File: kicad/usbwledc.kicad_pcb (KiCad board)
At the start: 2 copper layers, 30 x 35 mm, 31 parts, among them J1 5V PAD, J10 USB_C_Receptacle_USB2.0, J2 D1 PAD, J3 GND PAD, J4 5V PAD, J5 D2 PAD, J6 GND PAD, J7 Accessories, SW1 FLASH_SW, U1 CH340N, U2 AMS1117-3.3, U3 ESP32-WROOM-32

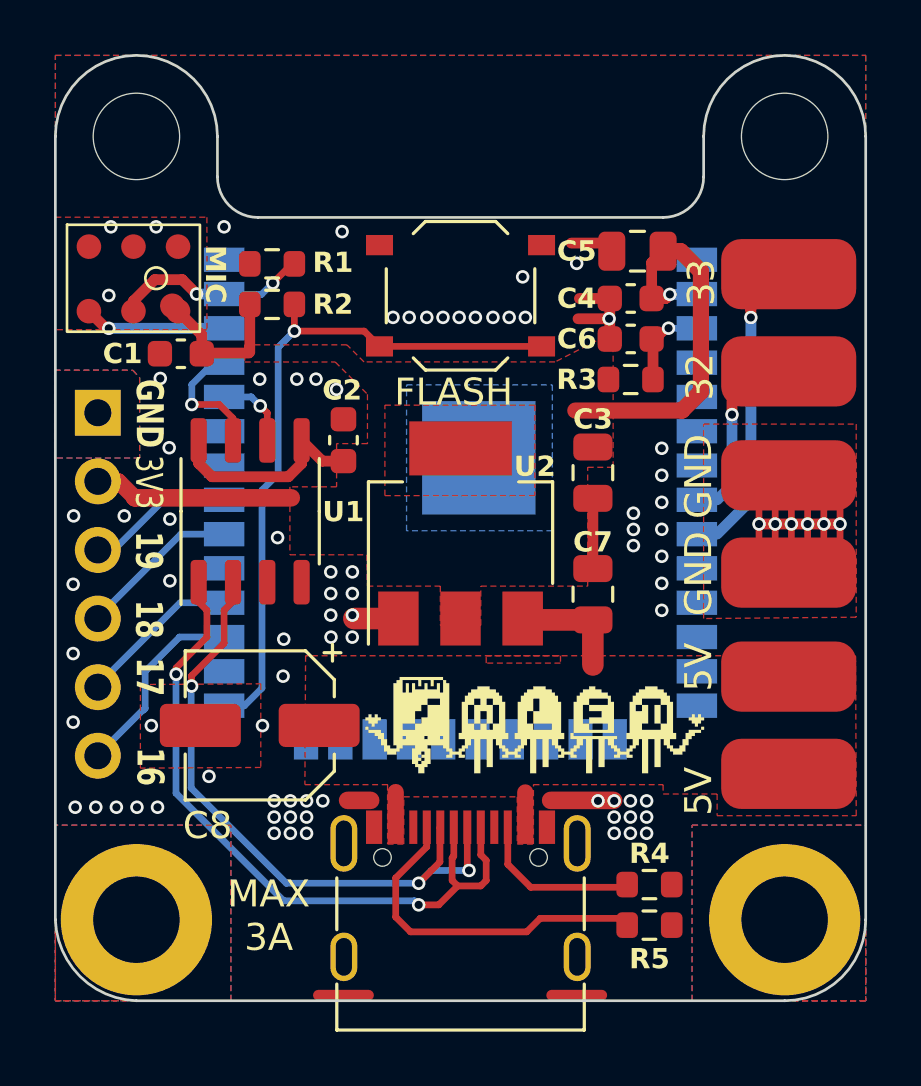
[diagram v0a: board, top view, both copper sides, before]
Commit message: Replaced MEMS mic to a curent available version.
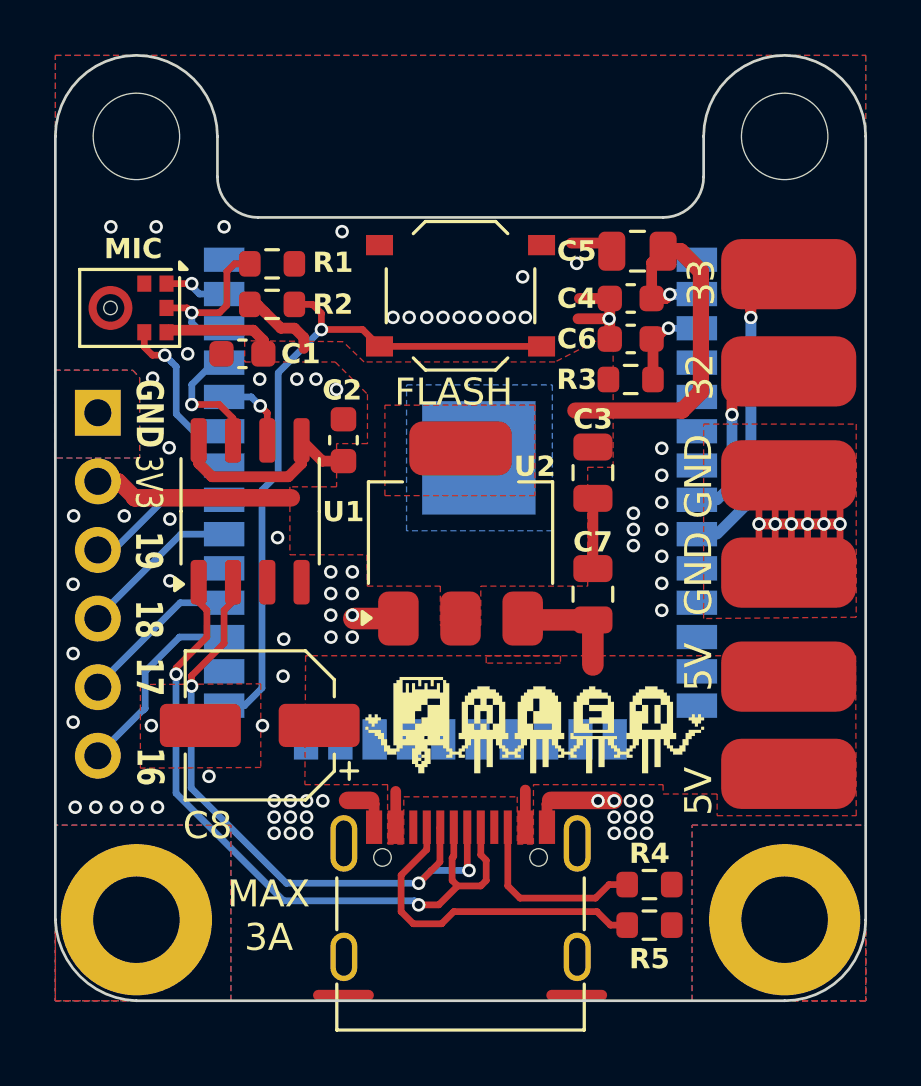
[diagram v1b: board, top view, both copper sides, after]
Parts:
- MK1: value GSA4737 -> ICS-43434; footprint microphone:Microphone-6pin -> Sensor_Audio:InvenSense_ICS-43434-6_3.5x2.65mm
- moved MK1 3.71 mm to (32.8, 39.4)
- moved C1 2.28 mm to (36.9, 41.0), turned to 0 degrees
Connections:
- C1 pad 1: +3V3 -> GND
- C1 pad 2: GND -> +3V3
- MK1 pad 1: GND -> I2S_WS
- MK1 pad 2: unconnected-(MK1-WS-Pad2) -> GND
- MK1 pad 5: I2S_SD -> +3V3
- MK1 pad 6: +3V3 -> I2S_SD
- R1 pad 1: GND -> I2S_SD
- R1 pad 2: I2S_SD -> GND
- U3 pad 12: RELAY -> unconnected-(U3-IO27-Pad12)
- U3 pad 33: unconnected-(U3-IO21-Pad33) -> I2S_SCK
- U3 pad 36: I2S_SCK -> I2S_SD
- U3 pad 37: I2S_SD -> I2S_WS
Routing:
- net I2S_WS: track 0.00 -> 2.35 mm, vias 0 -> 1
- net GND: track 27.0 -> 29.1 mm
- net +3V3: track 35.4 -> 37.2 mm
- net I2S_SD: track 7.36 -> 6.30 mm, vias 2 -> 1
- net Net-(J10-CC2): track 6.19 -> 7.13 mm
- net I2S_SCK: track 5.27 -> 5.82 mm
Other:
- board text added: "v1.2"
- board text removed: "22"
- board text removed: "23"
- board text removed: "NANDXOR"
- board text removed: "SD"
- board text removed: "WS"
- board text removed: "v1.1"
